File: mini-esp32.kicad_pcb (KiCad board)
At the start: 4 copper layers, 29 x 58 mm, 48 parts, among them J1 BAT, J2 USB_B_Micro, J5 Conn_01x18, J6 Conn_01x18, Q1 AO3401A, Q2 S8050, Q3 S8050, Q4 2N7002, Q5 AO3400A, Q6 AO3400A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

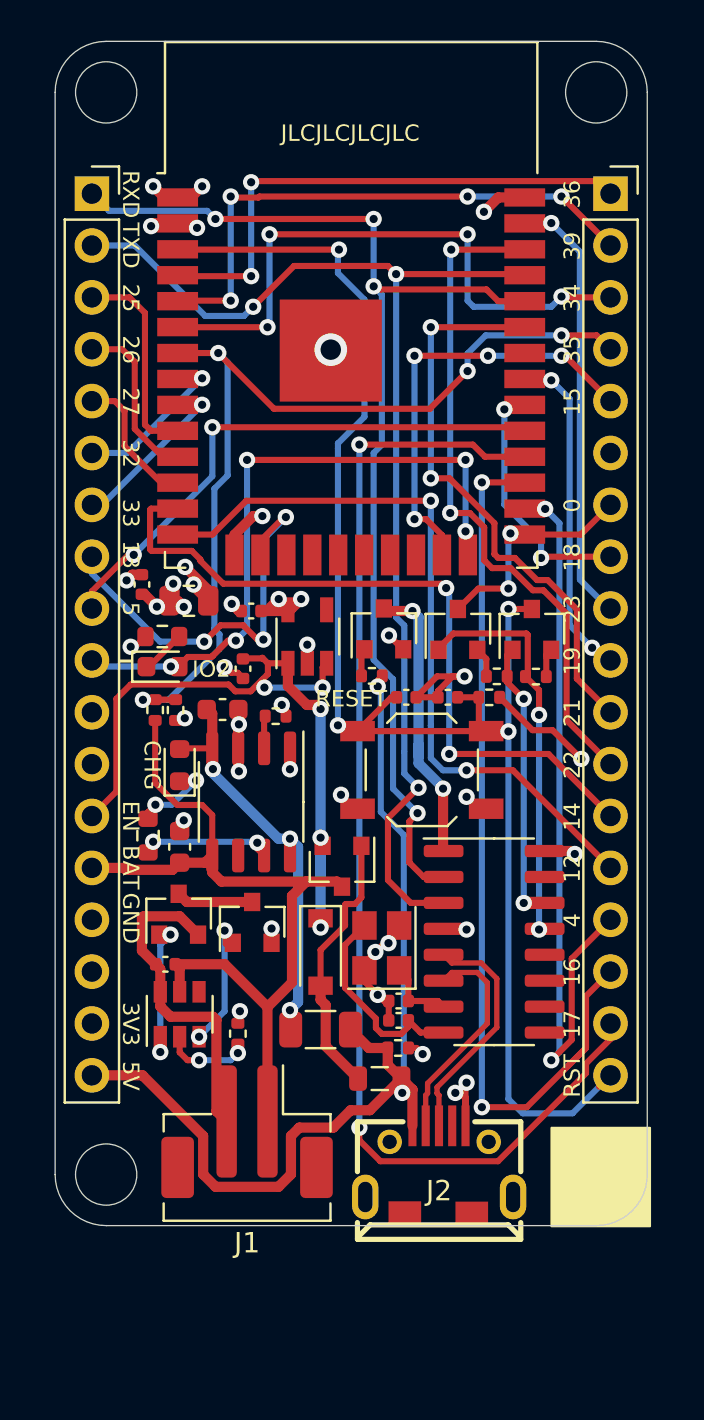
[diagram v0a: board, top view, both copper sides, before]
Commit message: Fix more critical bugs
Fix NPN transistor pin mapping.
Re-add LDO EN pin pull up resistor.
Fix battery protection IC wiring and components to recommendation.
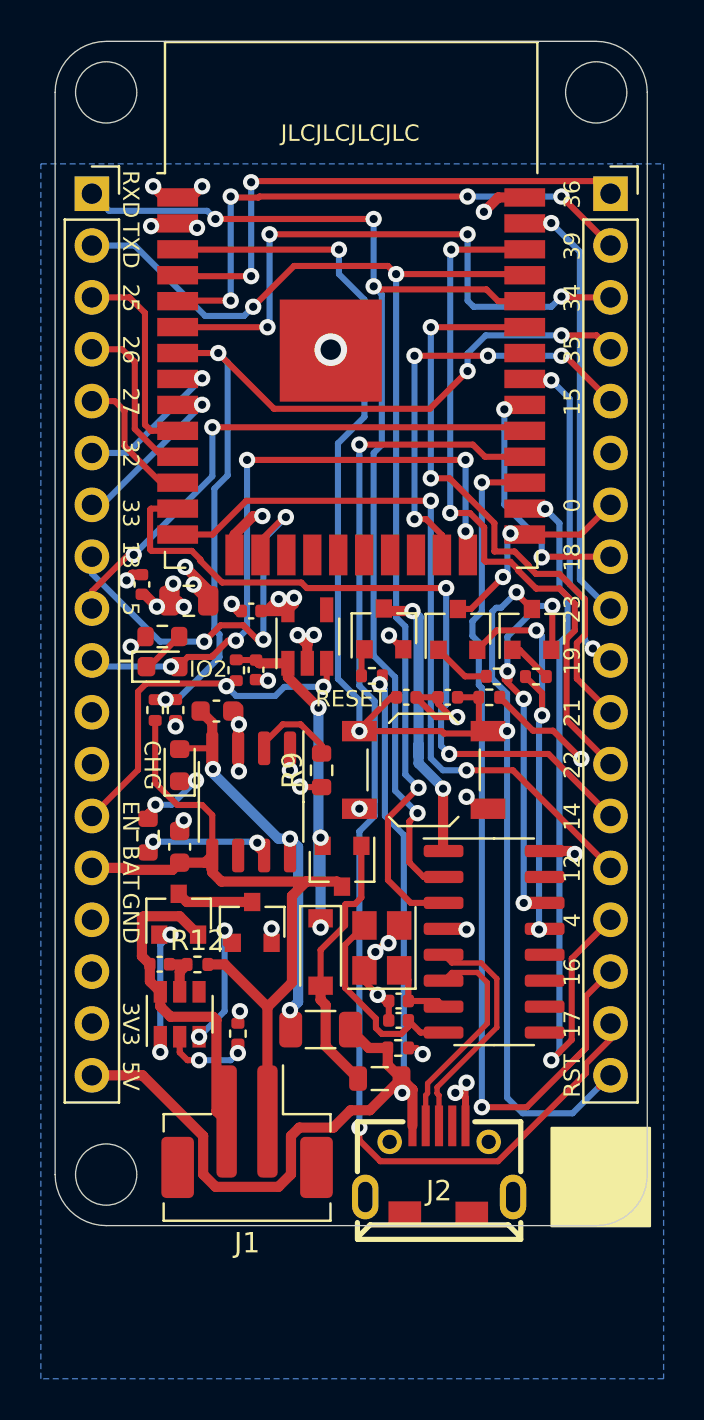
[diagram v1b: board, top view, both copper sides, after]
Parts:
- added R12: 100R, Resistor_SMD:R_0402_1005Metric, F.Cu at (126.2, 106.8)
- added R3: 10k, Resistor_SMD:R_0402_1005Metric, F.Cu at (128.1, 92.4)
- R15: value 2k -> 1k
- R9: footprint Resistor_SMD:R_0402_1005Metric -> Resistor_SMD:R_0603_1608Metric
- moved R9 3.48 mm to (132.2, 97.3), turned to 90 degrees
- moved C2 0.64 mm to (129.0, 92.4)
- moved C1 0.31 mm to (127.1, 94.4)
- moved C11 0.28 mm to (124.3, 106.8)
- moved SW1 0.09 mm to (137.2, 97.3)
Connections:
- C11 pad 1: BAT+ -> Net-(C11-Pad1)
- C2 pad 1: EN -> Net-(C2-Pad1)
- D1 pad 1: EN -> Net-(C2-Pad1)
- Q1 pad 2: EN -> Net-(C2-Pad1)
- Q2 pad 1: DTR -> Net-(Q2-Pad1)
- Q2 pad 2: Net-(Q2-Pad2) -> DTR
- Q3 pad 1: RTS -> Net-(Q3-Pad1)
- Q3 pad 2: Net-(Q3-Pad2) -> RTS
- R7 pad 1: Net-(Q2-Pad2) -> Net-(Q2-Pad1)
- R8 pad 1: Net-(Q3-Pad2) -> Net-(Q3-Pad1)
- U2 pad 1: EN -> Net-(C2-Pad1)
- U5 pad 5: BAT+ -> Net-(C11-Pad1)
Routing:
- net EN: track 39.0 -> 18.7 mm, vias 5 -> 2
- net Net-(C2-Pad1): track 0.00 -> 19.3 mm, vias 0 -> 3
- net RTS: track 13.9 -> 19.4 mm, vias 2 -> 4
- net BAT+: track 43.0 -> 39.9 mm
- net Net-(Q2-Pad1): track 0.00 -> 2.88 mm
- net Net-(R9-Pad2): track 1.60 -> 4.28 mm
- net Net-(C11-Pad1): track 0.00 -> 2.35 mm
- net Net-(Q3-Pad1): track 0.00 -> 2.20 mm
- net Net-(Q2-Pad2): track 1.48 -> 0.00 mm
- net RESET: track 78.3 -> 79.8 mm
- net Net-(Q3-Pad2): track 1.41 -> 0.00 mm
- net I35: track 46.0 -> 45.1 mm
- net IO22: track 33.5 -> 34.4 mm
- net IO21: track 28.4 -> 29.2 mm
- net DTR: track 19.9 -> 20.6 mm, vias 2 -> 3
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- added copper zone on B.Cu, net GND

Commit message: Fix CH340G. Backside pin numbering.
 - Crystal cap to 22pF from 33pf like the reference implementation.
 - Fix CH340G VCC to use an extra LDO instead of using RT9080 with a N MOSFET. N MOSFET to the GND seems to interfere with the CH340G's USB signalling.
 - Backside silkscreen pin numbering
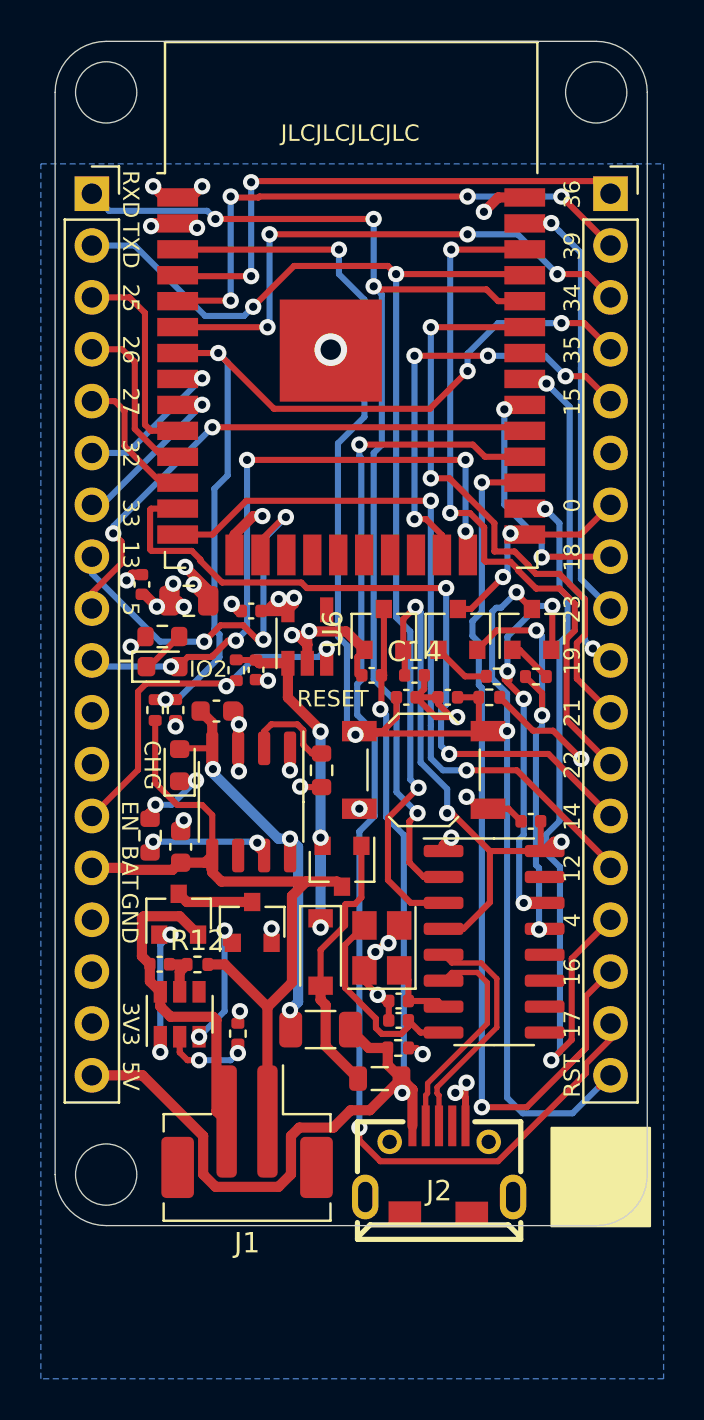
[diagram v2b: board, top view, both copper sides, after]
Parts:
- removed Q4: 2N7002, Package_TO_SOT_SMD:SOT-23
- removed R14: 100R, Resistor_SMD:R_0402_1005Metric
- added C12: 100n, Capacitor_SMD:C_0402_1005Metric, F.Cu at (142.5, 99.8)
- added C13: 1u, Capacitor_SMD:C_0402_1005Metric, F.Cu at (134.7, 92.7)
- added C14: 1u, Capacitor_SMD:C_0402_1005Metric, F.Cu at (136.8, 92.7)
- added U6: XC6206P332MR, Package_TO_SOT_SMD:SOT-23, F.Cu at (135.3, 90.4)
- C10, C9: value 33p -> 22p
- moved R4 0.10 mm to (123.8, 100.5)
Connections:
- U4 pad 1: CH340GND -> GND
- U4 pad 16: VDD -> CH340_VCC
- U4 pad 4: VDD -> CH340_VCC
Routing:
- net CH340_VCC: track 0.00 -> 27.8 mm, vias 0 -> 3
- net CH340GND: track 14.4 -> 0.00 mm, vias 2 -> 0
- net GND: track 41.2 -> 49.0 mm
- net VBUS: track 49.9 -> 53.3 mm
- net VDD: track 17.6 -> 14.9 mm, vias 10 -> 8
- net I34: track 29.3 -> 27.0 mm
- net Net-(Q4-Pad1): track 1.36 -> 0.00 mm
- net IO4: track 37.4 -> 37.9 mm
- net Net-(R9-Pad2): track 4.28 -> 4.79 mm
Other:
- board text added: "Mini ESP32 V3.0.1"
- board text removed: "Mini ESP32 V3.0"

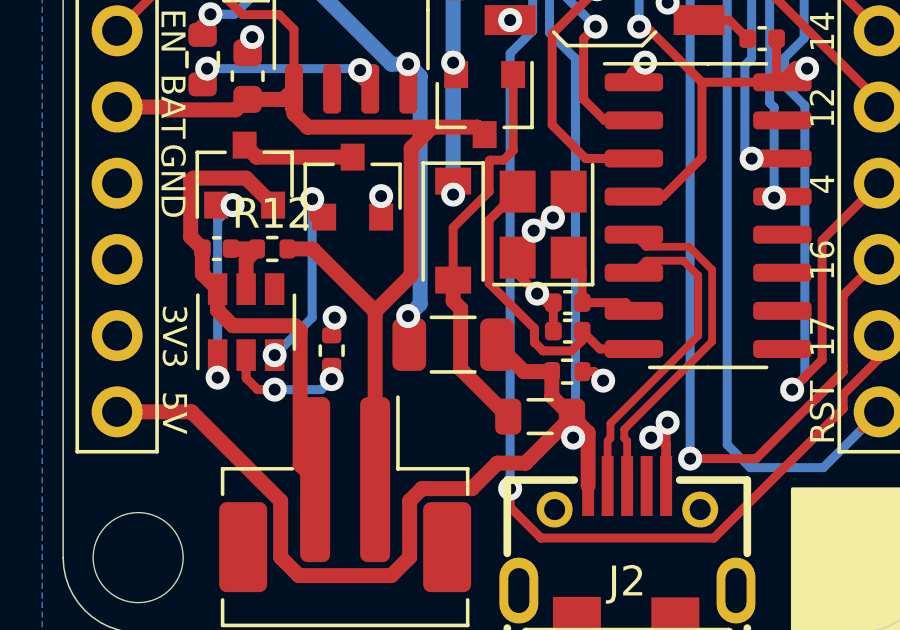
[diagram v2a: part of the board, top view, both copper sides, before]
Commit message: Change 0.1R TP4056 resistor to a diode
Helps with the heat issues of TP4056.
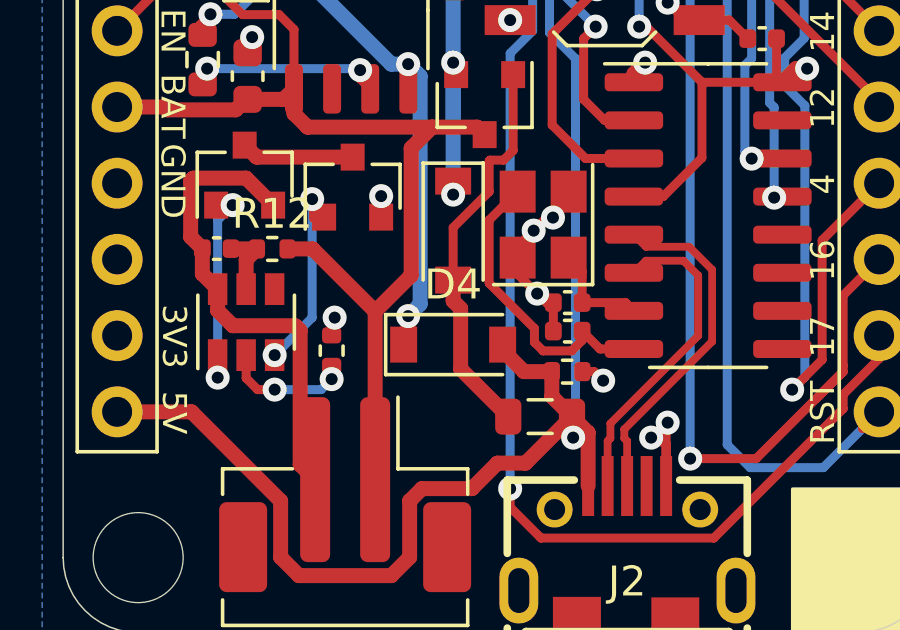
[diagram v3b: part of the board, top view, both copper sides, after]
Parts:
- removed R2: 0.1R, Resistor_SMD:R_1206_3216Metric
- added D4: B5819W, Diode_SMD:D_SOD-123, F.Cu at (132.2, 110.0)
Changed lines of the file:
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@@
-    )
-  )
-  (module Resistor_SMD:R_1206_3216Metric (layer F.Cu)
-    (at 132.2 110)
-    (descr "Resistor SMD 1206 (3216 Metric), square (rectangular) end terminal, IPC_7351 nominal, (Body size source: IPC-SM-782 page 72, https://www.pcb-3d.com/wordpress/wp-content/uploads/ipc-sm-782a_amendment_1_and_2.pdf), generated with kicad-footprint-generator")
-    (tags resistor)
-    (attr smd)
-    (fp_text reference R2 (at 0 -1.82) (layer F.Fab)
-      (effects (font (size 1 1) (thickness 0.15)))
-    )
-    (fp_text value 0.1R (at 0 1.82) (layer F.Fab)
-      (effects (font (size 1 1) (thickness 0.15)))
-    )
-    (fp_line (start -1.6 0.8) (end -1.6 -0.8) (layer F.Fab) (width 0.1))
-    (fp_line (start -1.6 -0.8) (end 1.6 -0.8) (layer F.Fab) (width 0.1))
-    (fp_line (start 1.6 -0.8) (end 1.6 0.8) (layer F.Fab) (width 0.1))
-    (fp_line (start 1.6 0.8) (end -1.6 0.8) (layer F.Fab) (width 0.1))
-    (fp_line (start -0.727064 -0.91) (end 0.727064 -0.91) (layer F.SilkS) (width 0.12))
-    (fp_line (start -0.727064 0.91) (end 0.727064 0.91) (layer F.SilkS) (width 0.12))
-    (fp_line (start -2.28 1.12) (end -2.28 -1.12) (layer F.CrtYd) (width 0.05))
-    (fp_line (start -2.28 -1.12) (end 2.28 -1.12) (layer F.CrtYd) (width 0.05))
-    (fp_line (start 2.28 -1.12) (end 2.28 1.12) (layer F.CrtYd) (width 0.05))
-    (fp_line (start 2.28 1.12) (end -2.28 1.12) (layer F.CrtYd) (width 0.05))
-    (fp_text user %R (at 0 0) (layer F.Fab)
-      (effects (font (size 0.8 0.8) (thickness 0.12)))
-    )
-    (pad 2 smd roundrect (at 1.4625 0) (size 1.125 1.75) (layers F.Cu F.Paste F.Mask) (roundrect_rratio 0.2222195555555556)
-      (net 11 VBUS))
-    (pad 1 smd roundrect (at -1.4625 0) (size 1.125 1.75) (layers F.Cu F.Paste F.Mask) (roundrect_rratio 0.2222195555555556)
-      (net 1 "Net-(C1-Pad1)"))
-    (model ${KISYS3DMOD}/Resistor_SMD.3dshapes/R_1206_3216Metric.wrl
-      (at (xyz 0 0 0))
-      (scale (xyz 1 1 1))
-      (rotate (xyz 0 0 0))
     )
   )
@@
       (at (xyz 0 0 0))
       (scale (xyz 1 1 1))
+      (rotate (xyz 0 0 0))
+    )
+  )
+  (module Diode_SMD:D_SOD-123 (layer F.Cu)
+    (at 132.2 110)
+    (descr SOD-123)
+    (tags SOD-123)
+    (attr smd)
+    (fp_text reference D4 (at 0 -2) (layer F.SilkS)
+      (effects (font (size 1 1) (thickness 0.15)))
+    )
+    (fp_text value B5819W (at 0 2.1) (layer F.Fab)
+      (effects (font (size 1 1) (thickness 0.15)))
+    )
+    (fp_line (start -2.25 -1) (end 1.65 -1) (layer F.SilkS) (width 0.12))
+    (fp_line (start -2.25 1) (end 1.65 1) (layer F.SilkS) (width 0.12))
+    (fp_line (start -2.35 -1.15) (end -2.35 1.15) (layer F.CrtYd) (width 0.05))
+    (fp_line (start 2.35 1.15) (end -2.35 1.15) (layer F.CrtYd) (width 0.05))
+    (fp_line (start 2.35 -1.15) (end 2.35 1.15) (layer F.CrtYd) (width 0.05))
+    (fp_line (start -2.35 -1.15) (end 2.35 -1.15) (layer F.CrtYd) (width 0.05))
+    (fp_line (start -1.4 -0.9) (end 1.4 -0.9) (layer F.Fab) (width 0.1))
+    (fp_line (start 1.4 -0.9) (end 1.4 0.9) (layer F.Fab) (width 0.1))
+    (fp_line (start 1.4 0.9) (end -1.4 0.9) (layer F.Fab) (width 0.1))
+    (fp_line (start -1.4 0.9) (end -1.4 -0.9) (layer F.Fab) (width 0.1))
+    (fp_line (start -0.75 0) (end -0.35 0) (layer F.Fab) (width 0.1))
+    (fp_line (start -0.35 0) (end -0.35 -0.55) (layer F.Fab) (width 0.1))
+    (fp_line (start -0.35 0) (end -0.35 0.55) (layer F.Fab) (width 0.1))
+    (fp_line (start -0.35 0) (end 0.25 -0.4) (layer F.Fab) (width 0.1))
+    (fp_line (start 0.25 -0.4) (end 0.25 0.4) (layer F.Fab) (width 0.1))
+    (fp_line (start 0.25 0.4) (end -0.35 0) (layer F.Fab) (width 0.1))
+    (fp_line (start 0.25 0) (end 0.75 0) (layer F.Fab) (width 0.1))
+    (fp_line (start -2.25 -1) (end -2.25 1) (layer F.SilkS) (width 0.12))
+    (fp_text user %R (at 0 -2) (layer F.Fab)
+      (effects (font (size 1 1) (thickness 0.15)))
+    )
+    (pad 1 smd rect (at -1.65 0) (size 0.9 1.2) (layers F.Cu F.Paste F.Mask)
+      (net 1 "Net-(C1-Pad1)"))
+    (pad 2 smd rect (at 1.65 0) (size 0.9 1.2) (layers F.Cu F.Paste F.Mask)
+      (net 11 VBUS))
+    (model ${KISYS3DMOD}/Diode_SMD.3dshapes/D_SOD-123.wrl
+      (at (xyz 0 0 0))
+      (scale (xyz 1 1 1))

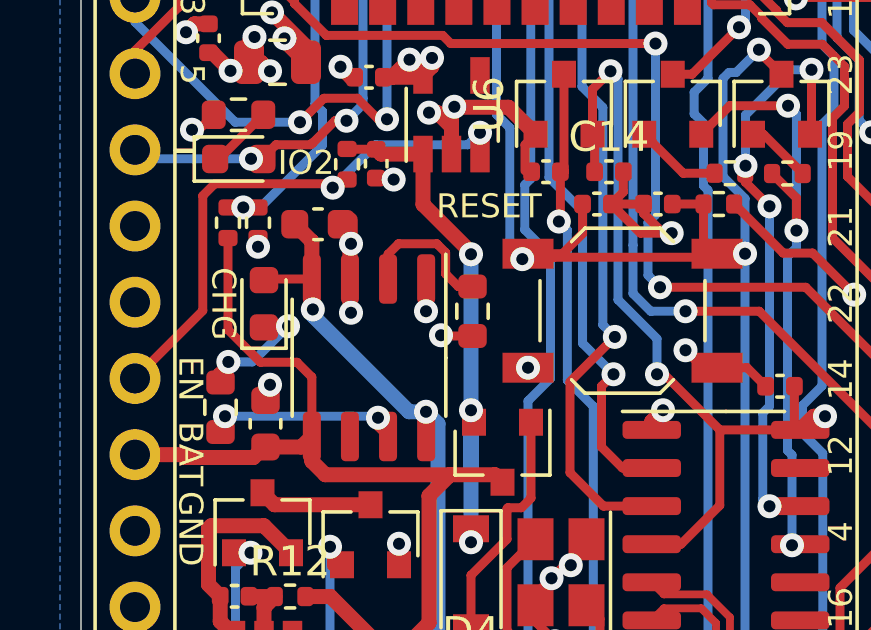
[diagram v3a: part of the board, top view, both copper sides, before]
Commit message: Extra GND heat dissipation for TP4056
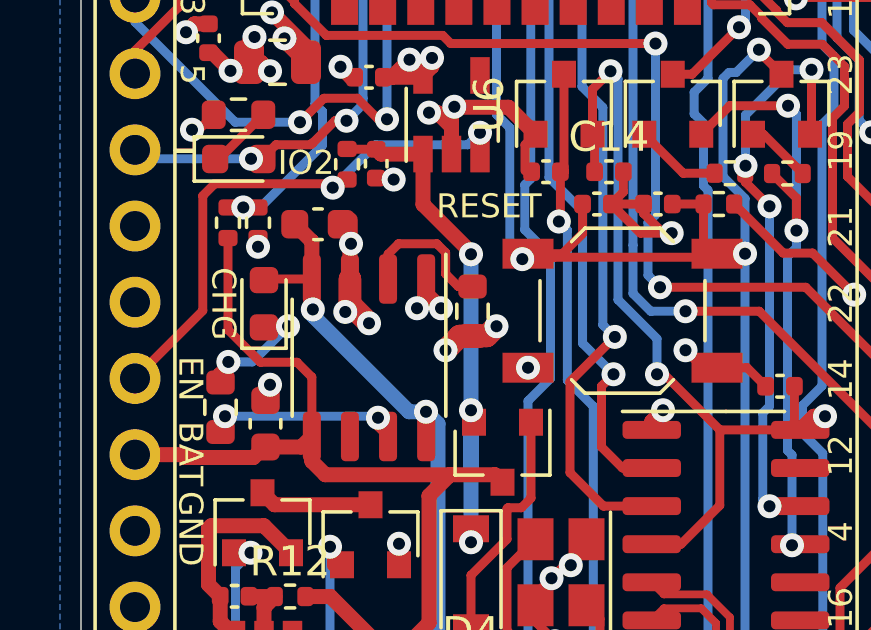
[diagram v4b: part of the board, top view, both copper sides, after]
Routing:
- net GND: track 49.0 -> 52.9 mm, vias 31 -> 34
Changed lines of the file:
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@@
     (thickness 1.6)
     (drawings 81)
-    (tracks 809)
+    (tracks 818)
     (zones 0)
     (modules 52)
@@
   )
   (setup
-    (last_trace_width 0.3)
+    (last_trace_width 0.75)
     (user_trace_width 0.3)
     (user_trace_width 0.5)
@@
   (via (at 122.9 91.25) (size 0.8) (drill 0.4) (layers F.Cu B.Cu) (net 2))
   (segment (start 122.964 91.186) (end 122.9 91.25) (width 0.3) (layer F.Cu) (net 2))
-  (via (at 128.2 97.35) (size 0.8) (drill 0.4) (layers F.Cu B.Cu) (net 2))
-  (segment (start 128.165 97.315) (end 128.2 97.35) (width 0.5) (layer F.Cu) (net 2))
-  (segment (start 128.165 96.225) (end 128.165 97.315) (width 0.5) (layer F.Cu) (net 2))
   (via (at 137.2 111.2) (size 0.8) (drill 0.4) (layers F.Cu B.Cu) (net 2))
   (segment (start 136.9 110.9) (end 137.2 111.2) (width 0.3) (layer F.Cu) (net 2))
@@
   (segment (start 134.1 99.182) (end 134.099997 99.181997) (width 0.3) (layer F.Cu) (net 2))
   (segment (start 134.01 99.182) (end 134.1 99.182) (width 0.3) (layer F.Cu) (net 2))
-  (via (at 131.2 98.1) (size 0.8) (drill 0.4) (layers F.Cu B.Cu) (net 2))
-  (segment (start 131.225 98.125) (end 131.2 98.1) (width 0.3) (layer F.Cu) (net 2))
-  (segment (start 132.25 98.125) (end 131.225 98.125) (width 0.3) (layer F.Cu) (net 2))
-  (via (at 130.7 97.3) (size 0.8) (drill 0.4) (layers F.Cu B.Cu) (net 2))
-  (segment (start 130.705 97.295) (end 130.7 97.3) (width 0.3) (layer F.Cu) (net 2))
-  (segment (start 130.705 96.225) (end 130.705 97.295) (width 0.3) (layer F.Cu) (net 2))
   (via (at 138.6 100.6) (size 0.8) (drill 0.4) (layers F.Cu B.Cu) (net 2))
   (segment (start 138.225 100.975) (end 138.6 100.6) (width 0.5) (layer F.Cu) (net 2))
@@
   (segment (start 131.55 91.15) (end 131.08 90.68) (width 0.5) (layer F.Cu) (net 2))
   (segment (start 131.08 90.68) (end 130.799984 90.68) (width 0.5) (layer F.Cu) (net 2))
+  (via (at 131.35 98.6) (size 0.8) (drill 0.4) (layers F.Cu B.Cu) (net 2))
+  (segment (start 131.825 98.125) (end 131.35 98.6) (width 0.75) (layer F.Cu) (net 2))
+  (segment (start 132.25 98.125) (end 131.825 98.125) (width 0.75) (layer F.Cu) (net 2))
+  (via (at 130.4 97.2) (size 0.8) (drill 0.4) (layers F.Cu B.Cu) (net 2))
+  (segment (start 130.705 96.895) (end 130.4 97.2) (width 0.5) (layer F.Cu) (net 2))
+  (segment (start 130.705 96.225) (end 130.705 96.895) (width 0.5) (layer F.Cu) (net 2))
+  (via (at 131.2 97.2) (size 0.8) (drill 0.4) (layers F.Cu B.Cu) (net 2))
+  (segment (start 130.705 96.705) (end 131.2 97.2) (width 0.5) (layer F.Cu) (net 2))
+  (segment (start 130.705 96.225) (end 130.705 96.705) (width 0.5) (layer F.Cu) (net 2))
+  (via (at 133.05 97.8) (size 0.8) (drill 0.4) (layers F.Cu B.Cu) (net 2))
+  (segment (start 132.725 98.125) (end 133.05 97.8) (width 0.75) (layer F.Cu) (net 2))
+  (segment (start 132.25 98.125) (end 132.725 98.125) (width 0.75) (layer F.Cu) (net 2))
+  (via (at 128.009135 97.322738) (size 0.8) (drill 0.4) (layers F.Cu B.Cu) (net 2))
+  (segment (start 128.165 97.166873) (end 128.009135 97.322738) (width 0.75) (layer F.Cu) (net 2))
+  (segment (start 128.165 96.225) (end 128.165 97.166873) (width 0.75) (layer F.Cu) (net 2))
+  (via (at 128.800008 97.700008) (size 0.8) (drill 0.4) (layers F.Cu B.Cu) (net 2))
+  (segment (start 128.165 97.065) (end 128.800008 97.700008) (width 0.75) (layer F.Cu) (net 2))
+  (segment (start 128.165 96.225) (end 128.165 97.065) (width 0.75) (layer F.Cu) (net 2))
   (via (at 132.2 105) (size 0.8) (drill 0.4) (layers F.Cu B.Cu) (net 3))
   (segment (start 132.2 104.55) (end 132.2 105) (width 0.5) (layer F.Cu) (net 3))
